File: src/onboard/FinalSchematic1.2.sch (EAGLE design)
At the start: 80 parts, among them IC1 MIC29310-5.0BT, IC3 A5975D

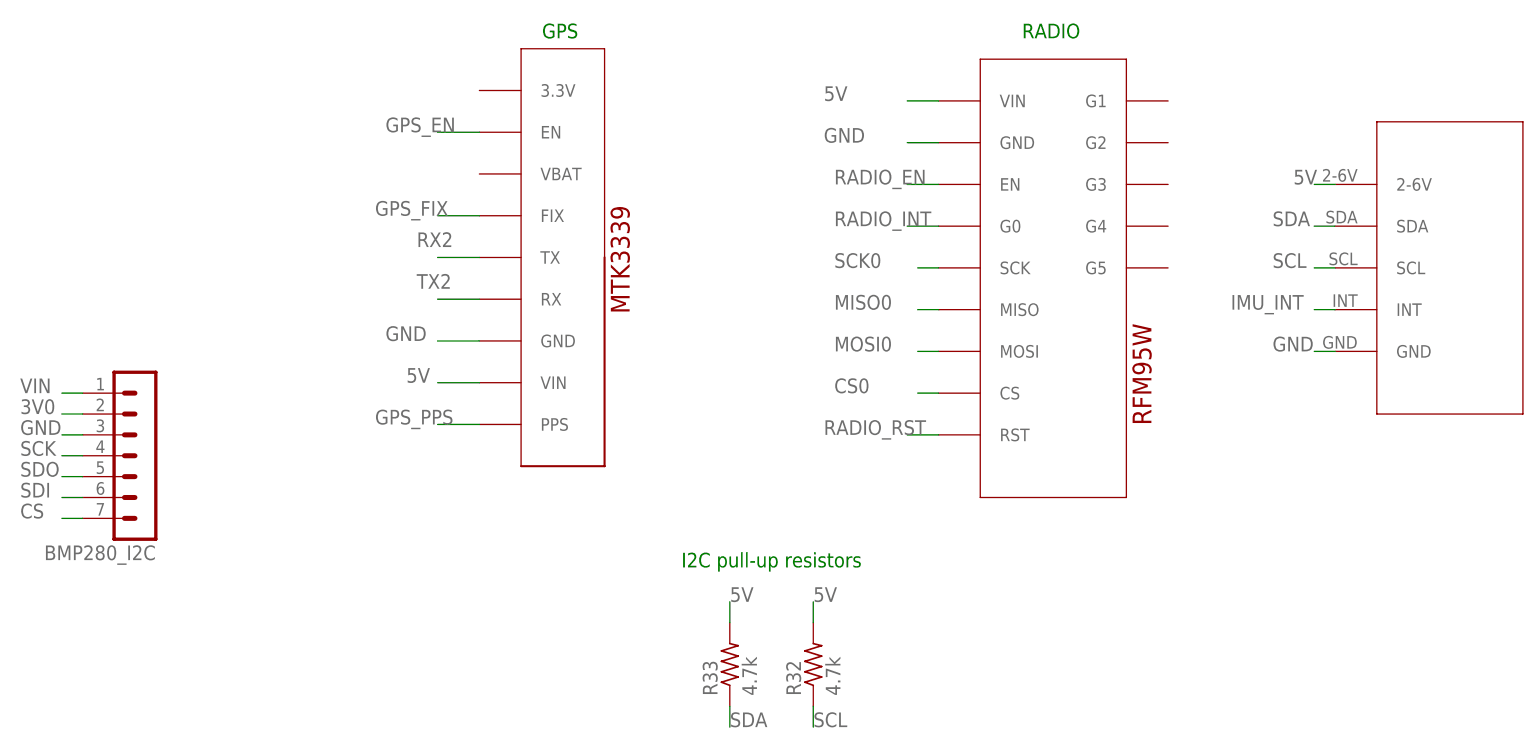
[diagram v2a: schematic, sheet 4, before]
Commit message: Added new BMP280 component to onboard
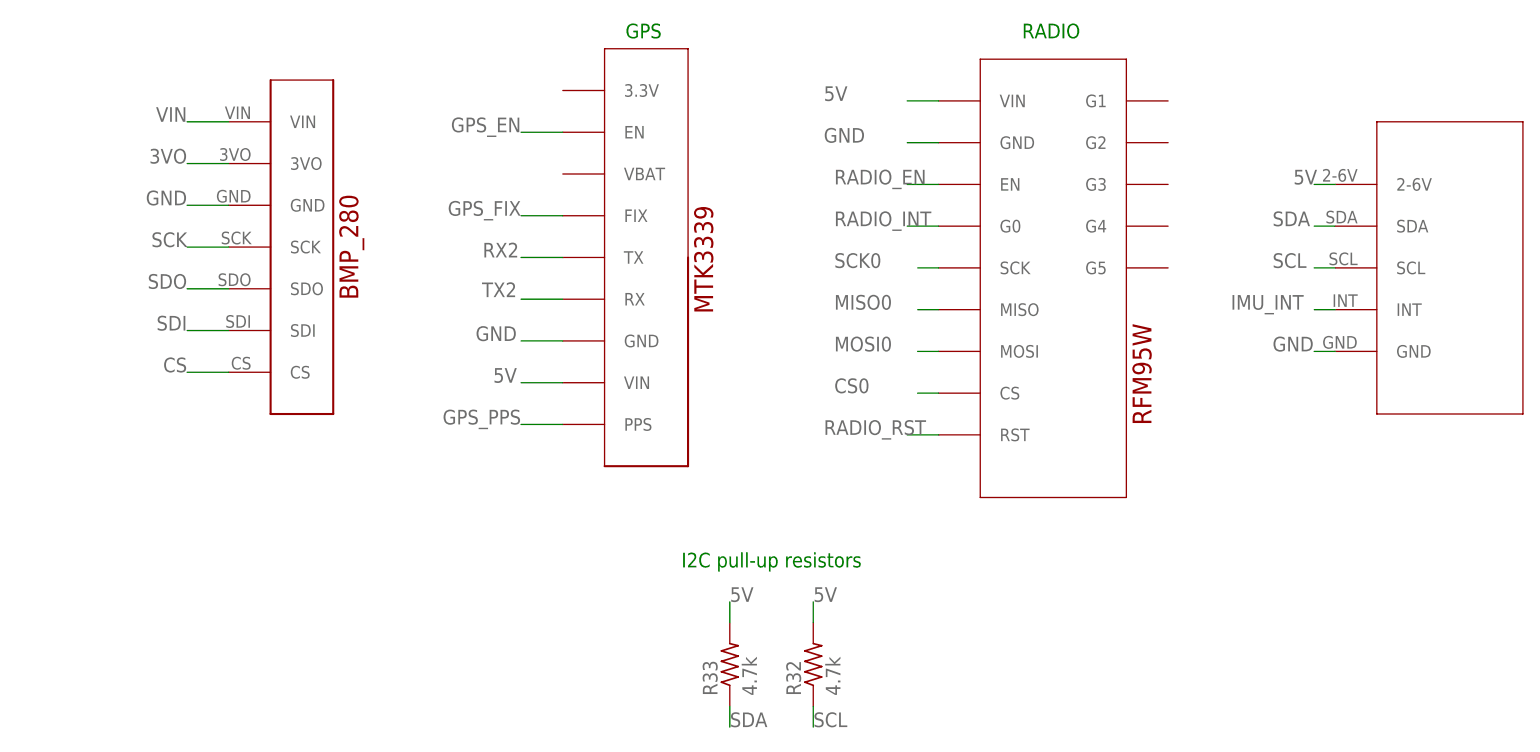
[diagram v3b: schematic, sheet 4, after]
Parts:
- removed BMP280_I2C: (no value), con-lstb:MA07-1
- added U1: ADAFRUIT_BMP280_BAROMETER, AERO_Eagle_Library:ADAFRUIT_BMP280_BAROMETER
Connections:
- removed net 3V0: BMP280_I2C.2
- new net 3VO: U1.3VO
- net CS: now also U1.CS; no longer BMP280_I2C.7
- net GND: now also U1.GND; no longer BMP280_I2C.3
- net SCK: now also U1.SCK; no longer BMP280_I2C.4
- net SDI: now also U1.SDI; no longer BMP280_I2C.6
- net SDO: now also U1.SDO; no longer BMP280_I2C.5
- net VIN: now also U1.VIN; no longer BMP280_I2C.1
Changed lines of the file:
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@@
 <part name="C2" library="capacitor-wima" library_urn="urn:adsk.eagle:library:116" deviceset="C" device="2,5-3" package3d_urn="urn:adsk.eagle:package:5436/1" value="10uF"/>
 <part name="GND16" library="supply1" library_urn="urn:adsk.eagle:library:371" deviceset="GND" device=""/>
-<part name="BMP280_I2C" library="con-lstb" library_urn="urn:adsk.eagle:library:162" deviceset="MA07-1" device="" package3d_urn="urn:adsk.eagle:package:8341/1"/>
+<part name="U1" library="AERO_Eagle_Library" deviceset="ADAFRUIT_BMP280_BAROMETER" device=""/>
 </parts>
 <sheets>
@@
 <plain>
 <text x="101.6" y="81.28" size="1.778" layer="91">RADIO</text>
-<text x="43.18" y="81.28" size="1.778" layer="91">GPS</text>
+<text x="53.34" y="81.28" size="1.778" layer="91">GPS</text>
 <text x="71.12" y="17.78" size="1.778" layer="91" align="center">I2C pull-up resistors</text>
 </plain>
 <instances>
-<instance part="GPSMTK3339" gate="G$1" x="48.26" y="80.01" smashed="yes" rot="R270"/>
+<instance part="GPSMTK3339" gate="G$1" x="58.42" y="80.01" smashed="yes" rot="R270"/>
 <instance part="RADIO" gate="G$1" x="96.52" y="78.74" smashed="yes" rot="R270"/>
 <instance part="IMU" gate="G$1" x="144.78" y="35.56" smashed="yes" rot="R270"/>
@@
 <attribute name="VALUE" x="69.342" y="1.27" size="1.778" layer="96" rot="R90"/>
 </instance>
-<instance part="BMP280_I2C" gate="1" x="-5.08" y="30.48" smashed="yes" rot="R180">
-<attribute name="VALUE" x="-3.81" y="43.18" size="1.778" layer="96" rot="R180"/>
-<attribute name="NAME" x="-3.81" y="19.558" size="1.778" layer="95" rot="R180"/>
-</instance>
+<instance part="U1" gate="G$1" x="17.78" y="76.2" smashed="yes" rot="R270"/>
 </instances>
 <busses>
@@
 <segment>
 <pinref part="GPSMTK3339" gate="G$1" pin="VIN"/>
-<wire x1="35.56" y1="39.37" x2="30.48" y2="39.37" width="0.1524" layer="91"/>
-<label x="26.67" y="39.37" size="1.778" layer="95"/>
+<wire x1="45.72" y1="39.37" x2="40.64" y2="39.37" width="0.1524" layer="91"/>
+<label x="40.132" y="39.37" size="1.778" layer="95" align="bottom-right"/>
 </segment>
 <segment>
@@
 <segment>
 <pinref part="GPSMTK3339" gate="G$1" pin="GND"/>
-<wire x1="35.56" y1="44.45" x2="30.48" y2="44.45" width="0.1524" layer="91"/>
-<label x="24.13" y="44.45" size="1.778" layer="95"/>
+<wire x1="45.72" y1="44.45" x2="40.64" y2="44.45" width="0.1524" layer="91"/>
+<label x="40.132" y="44.45" size="1.778" layer="95" align="bottom-right"/>
 </segment>
 <segment>
@@
 </segment>
 <segment>
-<pinref part="BMP280_I2C" gate="1" pin="3"/>
-<wire x1="-12.7" y1="33.02" x2="-15.24" y2="33.02" width="0.1524" layer="91"/>
-<label x="-20.32" y="33.02" size="1.778" layer="95"/>
+<pinref part="U1" gate="G$1" pin="GND"/>
+<wire x1="5.08" y1="60.96" x2="0" y2="60.96" width="0.1524" layer="91"/>
+<label x="0" y="60.96" size="1.778" layer="95" align="bottom-right"/>
 </segment>
 </net>
@@
 <segment>
 <pinref part="GPSMTK3339" gate="G$1" pin="EN"/>
-<wire x1="35.56" y1="69.85" x2="30.48" y2="69.85" width="0.1524" layer="91"/>
-<label x="24.13" y="69.85" size="1.778" layer="95"/>
+<wire x1="45.72" y1="69.85" x2="40.64" y2="69.85" width="0.1524" layer="91"/>
+<label x="40.64" y="69.85" size="1.778" layer="95" align="bottom-right"/>
 </segment>
 </net>
@@
 <segment>
 <pinref part="GPSMTK3339" gate="G$1" pin="FIX"/>
-<wire x1="35.56" y1="59.69" x2="30.48" y2="59.69" width="0.1524" layer="91"/>
-<label x="22.86" y="59.69" size="1.778" layer="95"/>
+<wire x1="45.72" y1="59.69" x2="40.64" y2="59.69" width="0.1524" layer="91"/>
+<label x="40.64" y="59.69" size="1.778" layer="95" align="bottom-right"/>
 </segment>
 </net>
@@
 <segment>
 <pinref part="GPSMTK3339" gate="G$1" pin="PPS"/>
-<wire x1="35.56" y1="34.29" x2="30.48" y2="34.29" width="0.1524" layer="91"/>
-<label x="22.86" y="34.29" size="1.778" layer="95"/>
+<wire x1="45.72" y1="34.29" x2="40.64" y2="34.29" width="0.1524" layer="91"/>
+<label x="40.64" y="34.29" size="1.778" layer="95" align="bottom-right"/>
 </segment>
 </net>
@@
 <segment>
 <pinref part="GPSMTK3339" gate="G$1" pin="TX"/>
-<wire x1="35.56" y1="54.61" x2="30.48" y2="54.61" width="0.1524" layer="91"/>
-<label x="27.94" y="55.88" size="1.778" layer="95"/>
+<wire x1="45.72" y1="54.61" x2="40.64" y2="54.61" width="0.1524" layer="91"/>
+<label x="40.386" y="54.61" size="1.778" layer="95" align="bottom-right"/>
 </segment>
 </net>
@@
 <segment>
 <pinref part="GPSMTK3339" gate="G$1" pin="RX"/>
-<wire x1="35.56" y1="49.53" x2="30.48" y2="49.53" width="0.1524" layer="91"/>
-<label x="27.94" y="50.8" size="1.778" layer="95"/>
+<wire x1="45.72" y1="49.53" x2="40.64" y2="49.53" width="0.1524" layer="91"/>
+<label x="40.132" y="49.784" size="1.778" layer="95" align="bottom-right"/>
 </segment>
 </net>
@@
 <net name="VIN" class="0">
 <segment>
-<pinref part="BMP280_I2C" gate="1" pin="1"/>
-<wire x1="-12.7" y1="38.1" x2="-15.24" y2="38.1" width="0.1524" layer="91"/>
-<label x="-20.32" y="38.1" size="1.778" layer="95"/>
-</segment>
-</net>
-<net name="3V0" class="0">
-<segment>
-<pinref part="BMP280_I2C" gate="1" pin="2"/>
-<wire x1="-12.7" y1="35.56" x2="-15.24" y2="35.56" width="0.1524" layer="91"/>
-<label x="-20.32" y="35.56" size="1.778" layer="95"/>
+<pinref part="U1" gate="G$1" pin="VIN"/>
+<wire x1="5.08" y1="71.12" x2="0" y2="71.12" width="0.1524" layer="91"/>
+<label x="0" y="71.12" size="1.778" layer="95" align="bottom-right"/>
 </segment>
 </net>
 <net name="SCK" class="0">
 <segment>
-<pinref part="BMP280_I2C" gate="1" pin="4"/>
-<wire x1="-12.7" y1="30.48" x2="-15.24" y2="30.48" width="0.1524" layer="91"/>
-<label x="-20.32" y="30.48" size="1.778" layer="95"/>
+<pinref part="U1" gate="G$1" pin="SCK"/>
+<wire x1="5.08" y1="55.88" x2="0" y2="55.88" width="0.1524" layer="91"/>
+<label x="0" y="55.88" size="1.778" layer="95" align="bottom-right"/>
 </segment>
 </net>
 <net name="SDO" class="0">
 <segment>
-<pinref part="BMP280_I2C" gate="1" pin="5"/>
-<wire x1="-12.7" y1="27.94" x2="-15.24" y2="27.94" width="0.1524" layer="91"/>
-<label x="-20.32" y="27.94" size="1.778" layer="95"/>
+<pinref part="U1" gate="G$1" pin="SDO"/>
+<wire x1="5.08" y1="50.8" x2="0" y2="50.8" width="0.1524" layer="91"/>
+<label x="0" y="50.8" size="1.778" layer="95" align="bottom-right"/>
 </segment>
 </net>
 <net name="SDI" class="0">
 <segment>
-<pinref part="BMP280_I2C" gate="1" pin="6"/>
-<wire x1="-12.7" y1="25.4" x2="-15.24" y2="25.4" width="0.1524" layer="91"/>
-<label x="-20.32" y="25.4" size="1.778" layer="95"/>
+<pinref part="U1" gate="G$1" pin="SDI"/>
+<wire x1="5.08" y1="45.72" x2="0" y2="45.72" width="0.1524" layer="91"/>
+<label x="0" y="45.72" size="1.778" layer="95" align="bottom-right"/>
 </segment>
 </net>
 <net name="CS" class="0">
 <segment>
-<pinref part="BMP280_I2C" gate="1" pin="7"/>
-<wire x1="-12.7" y1="22.86" x2="-15.24" y2="22.86" width="0.1524" layer="91"/>
-<label x="-20.32" y="22.86" size="1.778" layer="95"/>
-</segment>
-</net>
+<pinref part="U1" gate="G$1" pin="CS"/>
+<wire x1="5.08" y1="40.64" x2="0" y2="40.64" width="0.1524" layer="91"/>
+<label x="0" y="40.64" size="1.778" layer="95" align="bottom-right"/>
+</segment>
+</net>
+<net name="3VO" class="0">
+<segment>
+<pinref part="U1" gate="G$1" pin="3VO"/>
+<wire x1="5.08" y1="66.04" x2="0" y2="66.04" width="0.1524" layer="91"/>
+<label x="0" y="66.04" size="1.778" layer="95" align="bottom-right"/>
+</segment>
+</net>

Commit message: First routing attempt Still need to fix silkscreen
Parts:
- removed SV16: (no value), con-lstb:MA03-1
- added C4: 10uF, capacitor-wima:C2,5-3
- added SV0: (no value), con-lstb:MA03-1
- renumbered TP1 to 5V, TP2 to SDA, TP3 to SCL, TP4 to 22V, TP5 to 6V
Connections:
- removed net 22_INPUT: R1.2
- removed net 3VO: U1.3VO
- removed net CS: U1.CS
- removed net SCK: U1.SCK
- removed net SDI: U1.SDI
- removed net SDO: U1.SDO
- removed net VIN: U1.VIN
- net 22V_INPUT: now also R1.2
- net 5V: now also SV0.2, U1.VIN; no longer SV16.2
- net 6V: now also C4.1
- net BTN1: no longer TEENSY4.1.24-A10/TX6/SCL2
- net BTN2: no longer TEENSY4.1.25-A11/RX6/SDA2
- net GND: now also C4.2, SV0.3; no longer SV16.3
- net N$100: now also SV0.1; no longer SV14.1
- net N$105: now also SV4.1; no longer SV11.1
- net N$108: now also SV5.1; no longer SV10.1
- net N$109: now also SV9.1; no longer SV5.1
- net N$112: now also SV15.1; no longer SV9.1
- net N$115: now also SV14.1; no longer SV6.1
- net N$118: now also SV13.1; no longer SV4.1
- net N$2: now also SV12.1; no longer SV3.1
- net N$43: now also SV11.1; no longer SV16.1
- net N$81: now also SV7.1; no longer SV13.1
- net N$82: now also SV3.1; no longer SV15.1
- net N$85: now also SV2.1; no longer SV8.1
- net N$88: now also SV6.1; no longer SV7.1
- net N$91: now also SV10.1; no longer SV2.1
- net N$94: now also SV8.1; no longer SV1.1
- net N$97: now also SV1.1; no longer SV12.1
- net O_LED: now also TEENSY4.1.41-A17/MISO1; no longer TEENSY4.1.40-A16/CS1
- net PWM0: now also R5.1; no longer R4.1
- net PWM1: now also R2.1; no longer R3.1
- net PWM11: now also R10.1; no longer R12.1
- net PWM14: now also R17.1; no longer R16.1
- net PWM15: now also R16.1; no longer R17.1
- net PWM2: now also R3.1; no longer R2.1
- net PWM3: now also R4.1; no longer R15.1
- net PWM4: now also R9.1; no longer R5.1
- net PWM5: now also R8.1; no longer R6.1
- net PWM7: now also R6.1; no longer R8.1
- net PWM8: now also R15.1; no longer R9.1
- net PWM9: now also R12.1; no longer R10.1
- net R_LED: now also TEENSY4.1.38-A14/CS/IN1; no longer TEENSY4.1.41-A17/MISO1
- net SCL: now also U1.SCK
- net SDA: now also U1.SDI
- net SELECT_PIN: now also TEENSY4.1.31-CTX3; no longer TEENSY4.1.2-OUT2
- net W_LED: now also TEENSY4.1.40-A16/CS1; no longer TEENSY4.1.38-A14/CS/IN1

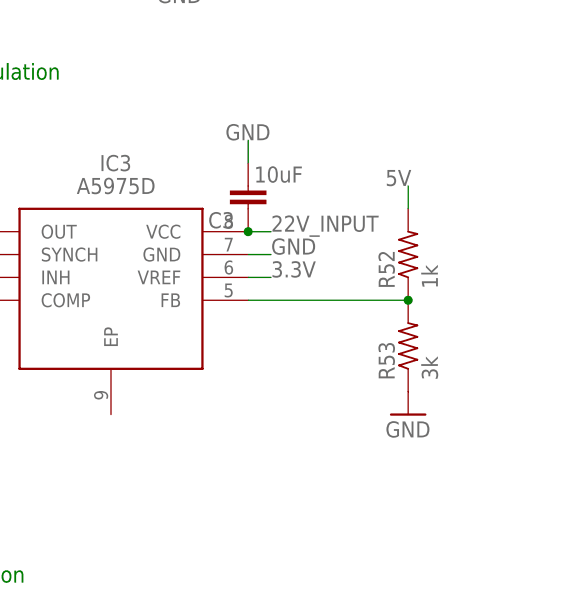
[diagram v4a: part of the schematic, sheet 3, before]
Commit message: Added 3.3 solderpad
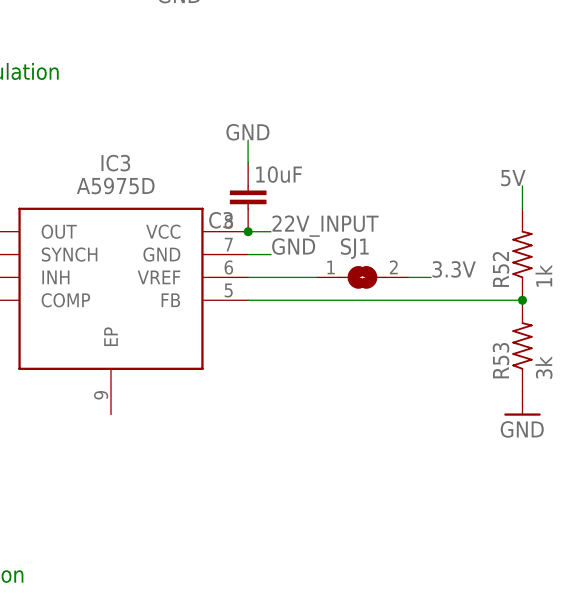
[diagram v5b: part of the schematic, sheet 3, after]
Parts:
- added SJ1: (no value), jumper:SJ
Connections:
- new net N$3: IC3.VREF, SJ1.1
- net 3.3V: now also SJ1.2; no longer IC3.VREF
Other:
- moved on the sheet: R52, R53
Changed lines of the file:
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@@
 <part name="GND19" library="supply1" library_urn="urn:adsk.eagle:library:371" deviceset="GND" device=""/>
 <part name="C4" library="capacitor-wima" library_urn="urn:adsk.eagle:library:116" deviceset="C" device="2,5-3" package3d_urn="urn:adsk.eagle:package:5436/1" value="10uF"/>
+<part name="SJ1" library="jumper" library_urn="urn:adsk.eagle:library:252" deviceset="SJ" device="" package3d_urn="urn:adsk.eagle:package:15471/1"/>
 </parts>
 <sheets>
@@
 <attribute name="VALUE" x="11.684" y="15.621" size="1.778" layer="96"/>
 </instance>
-<instance part="R52" gate="G$1" x="78.74" y="30.48" smashed="yes" rot="R90">
-<attribute name="NAME" x="77.2414" y="26.67" size="1.778" layer="95" rot="R90"/>
-<attribute name="VALUE" x="82.042" y="26.67" size="1.778" layer="96" rot="R90"/>
-</instance>
-<instance part="R53" gate="G$1" x="78.74" y="20.32" smashed="yes" rot="R90">
-<attribute name="NAME" x="77.2414" y="16.51" size="1.778" layer="95" rot="R90"/>
-<attribute name="VALUE" x="82.042" y="16.51" size="1.778" layer="96" rot="R90"/>
-</instance>
-<instance part="GND20" gate="1" x="78.74" y="12.7" smashed="yes">
-<attribute name="VALUE" x="76.2" y="10.16" size="1.778" layer="96"/>
+<instance part="R52" gate="G$1" x="91.44" y="30.48" smashed="yes" rot="R90">
+<attribute name="NAME" x="89.9414" y="26.67" size="1.778" layer="95" rot="R90"/>
+<attribute name="VALUE" x="94.742" y="26.67" size="1.778" layer="96" rot="R90"/>
+</instance>
+<instance part="R53" gate="G$1" x="91.44" y="20.32" smashed="yes" rot="R90">
+<attribute name="NAME" x="89.9414" y="16.51" size="1.778" layer="95" rot="R90"/>
+<attribute name="VALUE" x="94.742" y="16.51" size="1.778" layer="96" rot="R90"/>
+</instance>
+<instance part="GND20" gate="1" x="91.44" y="12.7" smashed="yes">
+<attribute name="VALUE" x="88.9" y="10.16" size="1.778" layer="96"/>
 </instance>
 <instance part="GND6" gate="1" x="10.16" y="10.16" smashed="yes">
@@
 <attribute name="NAME" x="6.604" y="-22.479" size="1.778" layer="95"/>
 <attribute name="VALUE" x="6.604" y="-27.559" size="1.778" layer="96"/>
+</instance>
+<instance part="SJ1" gate="1" x="73.66" y="27.94" smashed="yes">
+<attribute name="NAME" x="71.12" y="30.48" size="1.778" layer="95"/>
+<attribute name="VALUE" x="71.12" y="24.13" size="1.778" layer="96"/>
 </instance>
 </instances>
@@
 <segment>
 <pinref part="R52" gate="G$1" pin="2"/>
-<wire x1="78.74" y1="35.56" x2="78.74" y2="38.1" width="0.1524" layer="91"/>
-<label x="76.2" y="38.1" size="1.778" layer="95"/>
+<wire x1="91.44" y1="35.56" x2="91.44" y2="38.1" width="0.1524" layer="91"/>
+<label x="88.9" y="38.1" size="1.778" layer="95"/>
 </segment>
 <segment>
@@
 </segment>
 </net>
-<net name="3.3V" class="0">
-<segment>
-<pinref part="IC3" gate="G$1" pin="VREF"/>
-<wire x1="60.96" y1="27.94" x2="63.5" y2="27.94" width="0.1524" layer="91"/>
-<label x="63.5" y="27.94" size="1.778" layer="95"/>
-</segment>
-</net>
 <net name="GND" class="0">
 <segment>
@@
 <pinref part="R52" gate="G$1" pin="1"/>
 <pinref part="R53" gate="G$1" pin="2"/>
-<junction x="78.74" y="25.4"/>
+<junction x="91.44" y="25.4"/>
 <pinref part="IC3" gate="G$1" pin="FB"/>
-<wire x1="60.96" y1="25.4" x2="78.74" y2="25.4" width="0.1524" layer="91"/>
+<wire x1="60.96" y1="25.4" x2="91.44" y2="25.4" width="0.1524" layer="91"/>
 </segment>
 </net>
@@
 </segment>
 </net>
+<net name="N$3" class="0">
+<segment>
+<pinref part="IC3" gate="G$1" pin="VREF"/>
+<pinref part="SJ1" gate="1" pin="1"/>
+<wire x1="60.96" y1="27.94" x2="68.58" y2="27.94" width="0.1524" layer="91"/>
+</segment>
+</net>
+<net name="3.3V" class="0">
+<segment>
+<pinref part="SJ1" gate="1" pin="2"/>
+<wire x1="78.74" y1="27.94" x2="81.28" y2="27.94" width="0.1524" layer="91"/>
+<label x="81.28" y="27.94" size="1.778" layer="95"/>
+</segment>
+</net>
